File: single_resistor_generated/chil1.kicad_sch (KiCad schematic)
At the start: 1 part

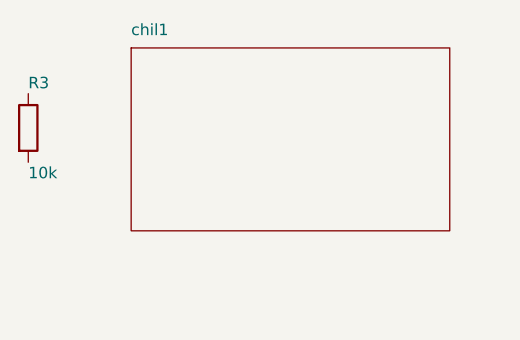
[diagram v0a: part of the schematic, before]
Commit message: adding updated testing code
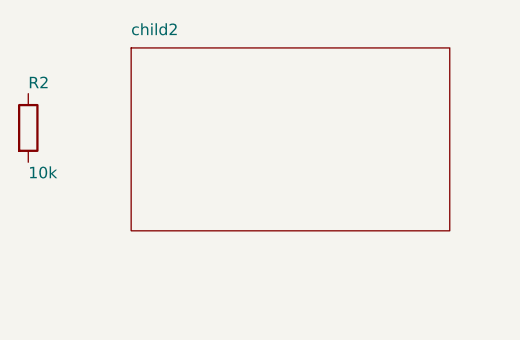
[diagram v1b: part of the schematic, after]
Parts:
- removed R3: 10k, Resistor_SMD:R_0603_1608Metric, symbol Device:R
- added R2: 10k, Resistor_SMD:R_0603_1608Metric, symbol Device:R
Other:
- removed sheet chil1
- added sheet child2 (child2.kicad_sch)
- title: singe_resistor_generated -> chil1
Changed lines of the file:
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@@
 	(paper "A4")
 	(title_block
-		(title singe_resistor_generated)
+		(title chil1)
 		(date 2025-08-04)
 		(company Circuit-Synth)
@@
 		(dnp no)
 		(fields_autoplaced yes)
-		(property "Reference" "R3"
+		(property "Reference" "R2"
 			(at 38.1 40.72 0)
 			(effects
@@
 		(instances
 			(project
-				""
+				"single_resistor_generated"
 				(path
-					"/4230698c-b526-4307-9655-afb80e239726"
-					(reference "R3")
+					"/4230698c-b526-4307-9655-afb80e239726/5eda4cf9-f3b7-4753-8ff9-af07e14d51ab/8b524237-4053-4f67-8c74-08cc3453a6a1"
+					(reference "R2")
 					(unit 1)
 				)
@@
 			)
 		)
-		(property "Sheetname" "chil1"
+		(property "Sheetname" "child2"
 			(at 49.53 35.559999999999995 0)
 			(effects
@@
 			)
 		)
-		(property "Sheetfile" "chil1.kicad_sch"
+		(property "Sheetfile" "child2.kicad_sch"
 			(at 49.53 58.42 0)
 			(effects
@@
 	(sheet_instances
 		(path
-			"/4230698c-b526-4307-9655-afb80e239726"
+			"/4230698c-b526-4307-9655-afb80e239726/5eda4cf9-f3b7-4753-8ff9-af07e14d51ab/8b524237-4053-4f67-8c74-08cc3453a6a1"
 			(page "1")
 		)
